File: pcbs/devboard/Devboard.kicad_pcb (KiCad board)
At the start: 2 copper layers, 11 parts, among them J1 Power, J2 Left, J3 ARM-JTAG, J4 Right, J5 JTAG, SW1 SW_Push, U1 Trådfri

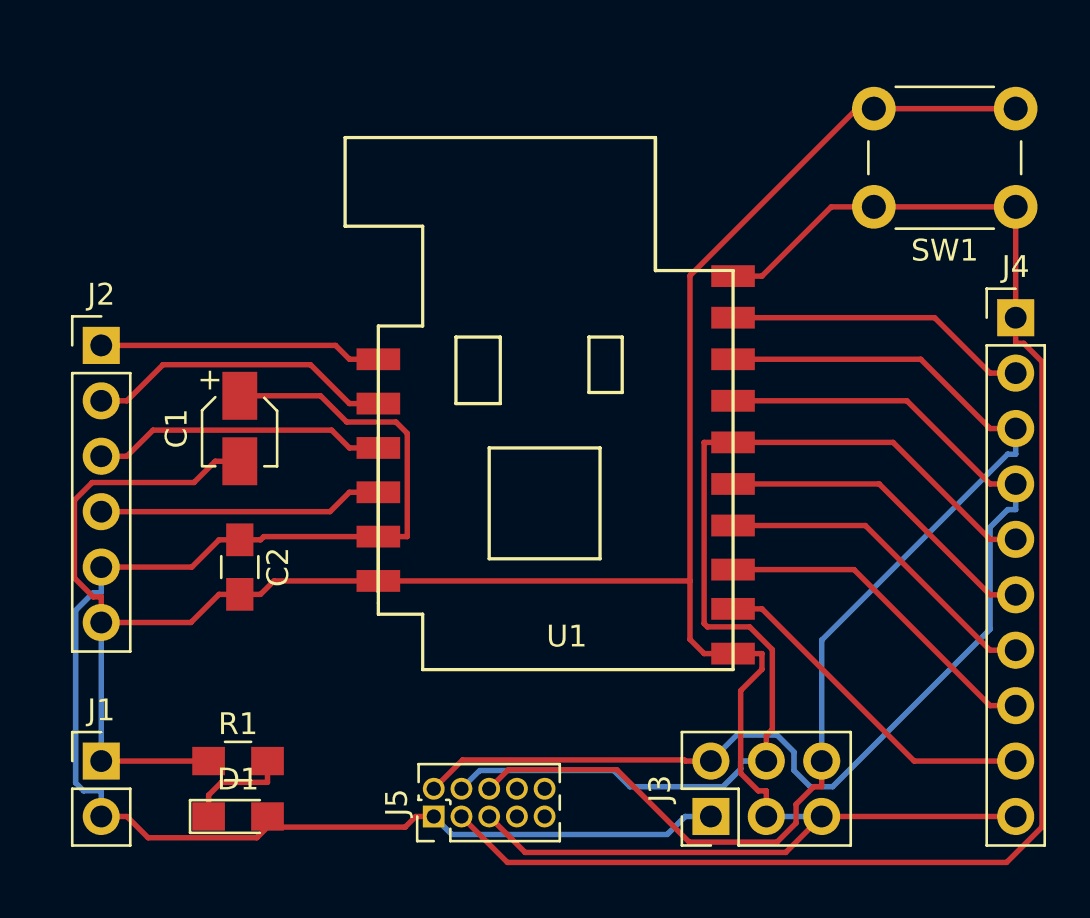
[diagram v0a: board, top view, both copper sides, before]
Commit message: Updated devboard pcb, accidentally swapped GND and VCC line.
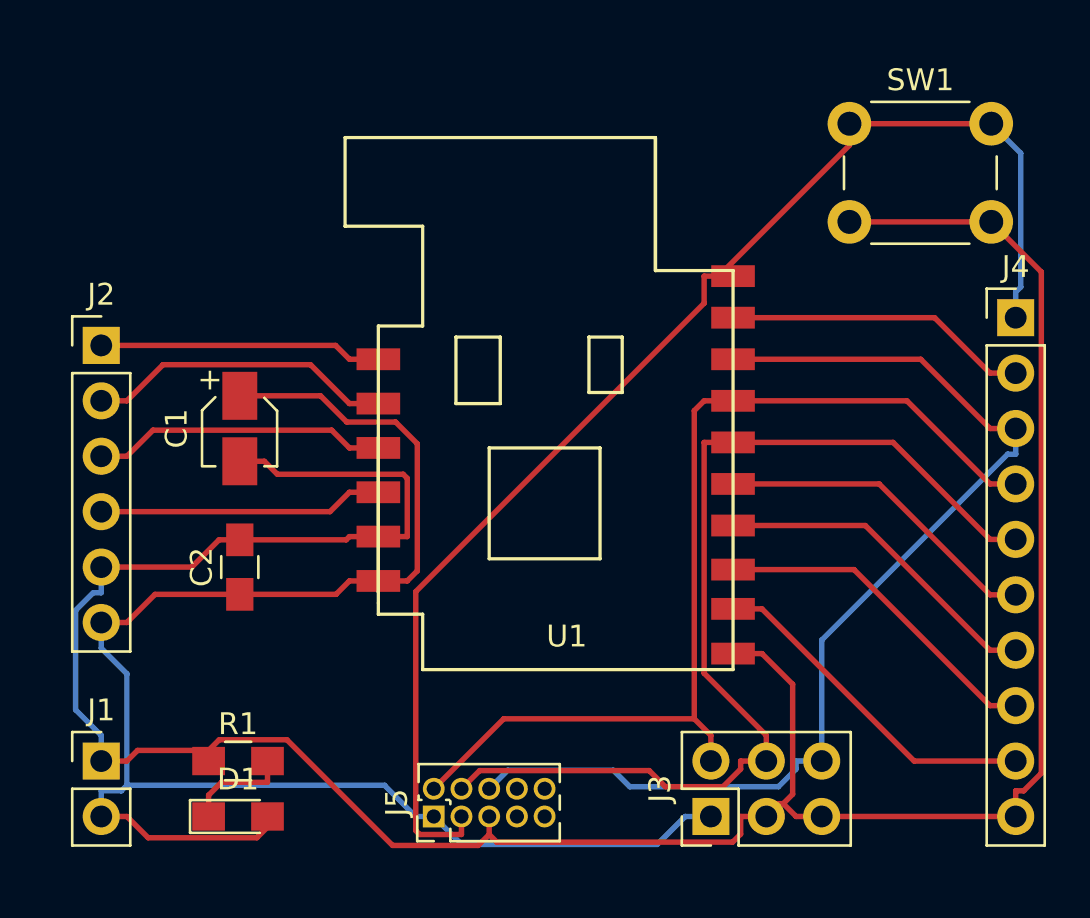
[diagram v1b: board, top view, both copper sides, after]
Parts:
- moved SW1 8.52 mm to (177.8, 95.2), turned to 0 degrees
- turned C2 to 90 degrees
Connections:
- J2 pad 5: +3V3 -> GND
- J2 pad 6: GND -> +3V3
- U1 pad 5: +3V3 -> GND
- U1 pad 6: GND -> +3V3
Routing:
- net /RESETn: track 71.6 -> 60.7 mm
- net +3V3: track 70.7 -> 77.9 mm
- net /SWDIO: track 52.9 -> 46.1 mm
- net /SWO: track 53.1 -> 50.0 mm
- net /SWCLK: track 48.6 -> 47.2 mm
- net GND: track 128.6 -> 127.5 mm

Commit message: Updated PCBs
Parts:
- J3: footprint Pin_Headers:Pin_Header_Straight_2x03_Pitch2.54mm -> Pin_Headers:Pin_Header_Straight_2x05_Pitch1.27mm
- J5: footprint Pin_Headers:Pin_Header_Straight_2x05_Pitch1.27mm -> Pin_Headers:Pin_Header_Straight_2x03_Pitch2.54mm
- U1: value Trådfri -> TRADFRI; footprint Parts:Trådfri PCB2.0 -> IKEA:TRADFRI_PCB2.0
- moved U1 12.0 mm to (166.7, 96.4)
- moved J4 4.44 mm to (181.0, 104.1)
- moved SW1 3.24 mm to (174.6, 94.6)
- moved J3 3.24 mm to (168.3, 126.4)
- moved C1 1.27 mm to (148.6, 109.2)
- moved C2 1.27 mm to (148.6, 115.6)
- moved D1 0.63 mm to (150.4, 127.0)
- moved J5 0.63 mm to (158.1, 127.0)
- moved R1 0.63 mm to (150.4, 124.5)
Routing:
- net GND: track 127.5 -> 110.3 mm
- net +3V3: track 77.9 -> 64.8 mm
- net /RESETn: track 60.7 -> 73.1 mm
- net /SWO: track 50.0 -> 41.5 mm
- net /SWCLK: track 47.2 -> 38.8 mm
- net /SWDIO: track 46.1 -> 42.0 mm
- net Net-(J4-Pad2): track 14.0 -> 10.9 mm
- net Net-(J4-Pad6): track 15.1 -> 12.2 mm
- net Net-(J4-Pad7): track 15.3 -> 12.5 mm
- net Net-(J4-Pad8): track 15.5 -> 12.8 mm
- net Net-(J4-Pad9): track 15.8 -> 13.2 mm
- net Net-(J2-Pad4): track 13.1 -> 10.4 mm
- net Net-(J2-Pad3): track 13.5 -> 11.1 mm
- net Net-(J2-Pad2): track 14.1 -> 11.7 mm
- net Net-(J2-Pad1): track 13.0 -> 10.6 mm
- added copper zone on B.Cu, net GND
- added copper zone on F.Cu, net GND
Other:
- board text added: "https://github.com/ basilfx/TRADFRI-Hacking"

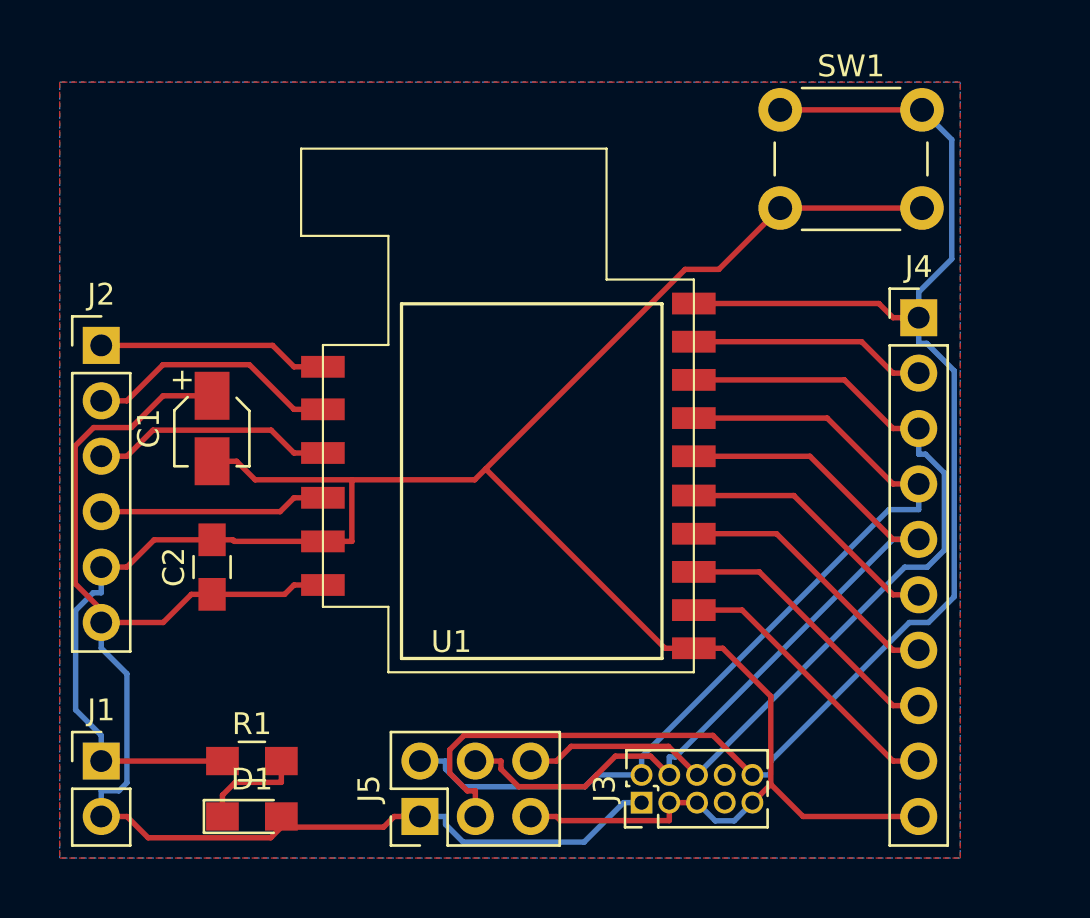
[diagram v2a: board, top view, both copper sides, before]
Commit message: Fixed edge cuts. Upgrade tot Kicad 5.0-rc2.
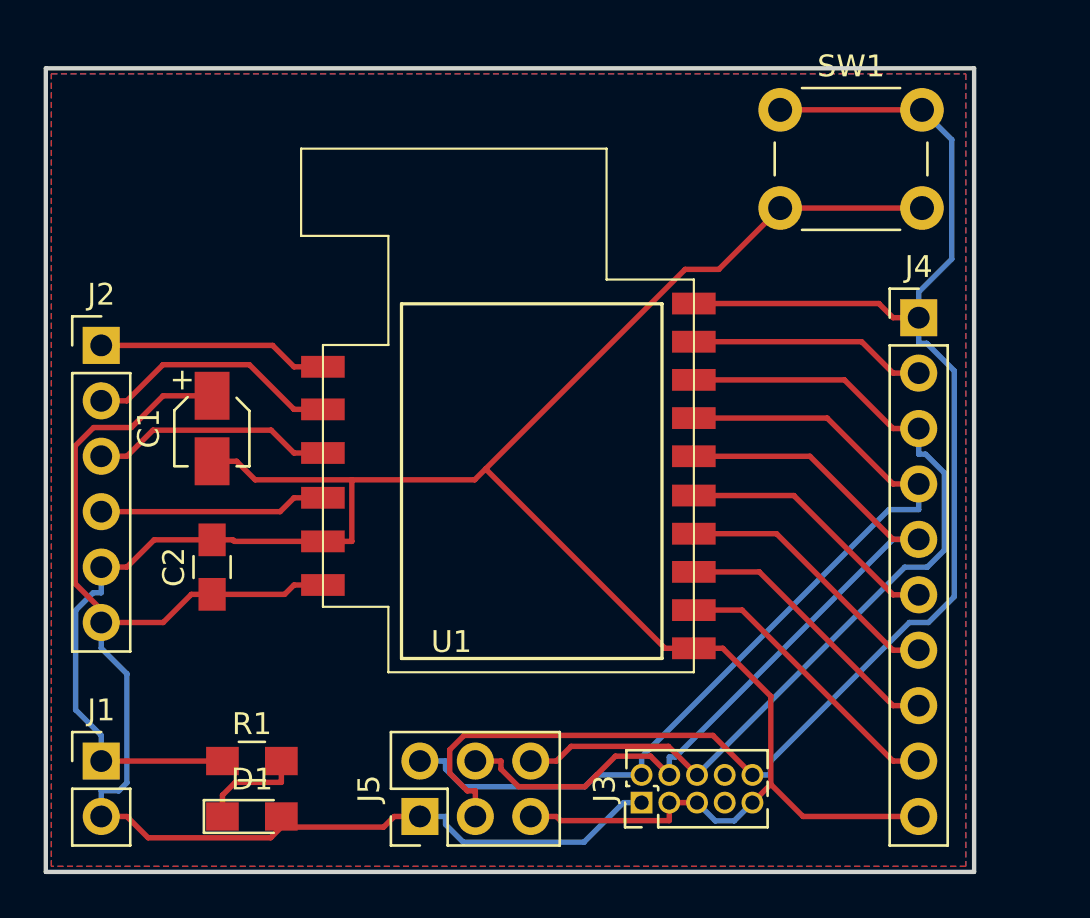
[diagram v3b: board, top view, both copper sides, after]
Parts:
- SW1: value SW_Push -> RESET
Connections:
- J3 pad 7: (no net) -> Net-(J3-Pad7)
- J3 pad 8: (no net) -> Net-(J3-Pad8)
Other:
- board outline added: 42.5 x 36.8 mm
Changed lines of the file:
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@@
-(kicad_pcb (version 4) (host pcbnew 4.0.7)
+(kicad_pcb (version 20171130) (host pcbnew "(5.0.0-rc2-dev-707-g2ed24a4)")
   (general
-    (links 44)
-    (no_connects 0)
-    (area 140.869999 91.64 183.615001 129.739524)
     (thickness 1.6)
     (drawings 5)
@@
     (zones 0)
     (modules 11)
-    (nets 17)
+    (nets 19)
   )
   (page A4)
@@
     (trace_min 0.2)
     (segment_width 0.2)
-    (edge_width 0.15)
+    (edge_width 0.2)
     (via_size 0.6)
     (via_drill 0.4)
@@
       (layerselection 0x00030_80000001)
       (usegerberextensions false)
+      (usegerberattributes false)
+      (usegerberadvancedattributes false)
+      (creategerberjobfile false)
       (excludeedgelayer true)
       (linewidth 0.100000)
@@
       (hpglpenspeed 20)
       (hpglpendiameter 15)
-      (hpglpenoverlay 2)
       (psnegative false)
       (psa4output false)
@@
   (net 15 "Net-(J4-Pad8)")
   (net 16 "Net-(J4-Pad9)")
+  (net 17 "Net-(J3-Pad7)")
+  (net 18 "Net-(J3-Pad8)")
   (net_class Default "Dit is de standaard class."
     (clearance 0.2)
@@
     (add_net "Net-(J2-Pad3)")
     (add_net "Net-(J2-Pad4)")
+    (add_net "Net-(J3-Pad7)")
+    (add_net "Net-(J3-Pad8)")
     (add_net "Net-(J4-Pad2)")
     (add_net "Net-(J4-Pad6)")
@@
       (effects (font (size 1 1) (thickness 0.15)))
     )
-    (fp_text value Left (at 0 15.03) (layer F.Fab)
+    (fp_text value Left (at -0.01 -2.51) (layer F.Fab)
       (effects (font (size 1 1) (thickness 0.15)))
     )
@@
       (effects (font (size 1 1) (thickness 0.15)))
     )
-    (fp_text value Right (at -2.54 21.59 90) (layer F.Fab)
+    (fp_text value Right (at -0.075 -2.74 180) (layer F.Fab)
       (effects (font (size 1 1) (thickness 0.15)))
     )
@@
       (effects (font (size 1 1) (thickness 0.15)))
     )
-    (fp_text value SW_Push (at 3.75 6.7) (layer F.Fab)
+    (fp_text value RESET (at -2.225 2.285 90) (layer F.Fab)
       (effects (font (size 1 1) (thickness 0.15)))
     )
@@
       (net 11 /RESETn))
     (model ${KISYS3DMOD}/Buttons_Switches_THT.3dshapes/SW_PUSH_6mm.wrl
-      (at (xyz 0.005 0 0))
+      (offset (xyz 0.1269999980926514 0 0))
       (scale (xyz 0.3937 0.3937 0.3937))
       (rotate (xyz 0 0 0))
@@
       (effects (font (size 1 1) (thickness 0.15)))
     )
-    (fp_text value ARM-JTAG (at 0.635 6.775 90) (layer F.Fab)
+    (fp_text value ARM-JTAG (at 3.565 2.625 180) (layer F.Fab)
       (effects (font (size 1 1) (thickness 0.15)))
     )
@@
     (pad 6 thru_hole oval (at 1.27 2.54 90) (size 1 1) (drill 0.65) (layers *.Cu *.Mask)
       (net 10 /SWO))
-    (pad 7 thru_hole oval (at 0 3.81 90) (size 1 1) (drill 0.65) (layers *.Cu *.Mask))
-    (pad 8 thru_hole oval (at 1.27 3.81 90) (size 1 1) (drill 0.65) (layers *.Cu *.Mask))
+    (pad 7 thru_hole oval (at 0 3.81 90) (size 1 1) (drill 0.65) (layers *.Cu *.Mask)
+      (net 17 "Net-(J3-Pad7)"))
+    (pad 8 thru_hole oval (at 1.27 3.81 90) (size 1 1) (drill 0.65) (layers *.Cu *.Mask)
+      (net 18 "Net-(J3-Pad8)"))
     (pad 9 thru_hole oval (at 0 5.08 90) (size 1 1) (drill 0.65) (layers *.Cu *.Mask)
       (net 1 GND))
@@
       (effects (font (size 1 1) (thickness 0.15)))
     )
-    (fp_text value JTAG (at 1.27 7.41 90) (layer F.Fab)
+    (fp_text value JTAG (at 5 2.485 180) (layer F.Fab)
       (effects (font (size 1 1) (thickness 0.15)))
     )
@@
     (effects (font (size 1.5 1.5) (thickness 0.3)) (justify mirror))
   )
-  (gr_line (start 183.515 92.71) (end 140.97 92.71) (layer B.CrtYd) (width 0.2))
-  (gr_line (start 183.515 129.54) (end 183.515 92.71) (layer B.CrtYd) (width 0.2))
-  (gr_line (start 140.97 129.54) (end 183.515 129.54) (layer B.CrtYd) (width 0.2))
-  (gr_line (start 140.97 92.71) (end 140.97 129.54) (layer B.CrtYd) (width 0.2))
+  (gr_line (start 183.515 92.71) (end 140.97 92.71) (layer Edge.Cuts) (width 0.2))
+  (gr_line (start 183.515 129.54) (end 183.515 92.71) (layer Edge.Cuts) (width 0.2))
+  (gr_line (start 140.97 129.54) (end 183.515 129.54) (layer Edge.Cuts) (width 0.2))
+  (gr_line (start 140.97 92.71) (end 140.97 129.54) (layer Edge.Cuts) (width 0.2))
   (segment (start 148.59 114.32) (end 149.5403 114.32) (width 0.25) (layer F.Cu) (net 1))
   (segment (start 164.5606 127.1903) (end 169.545 127.1903) (width 0.25) (layer F.Cu) (net 1))
@@
   (segment (start 170.67 117.541) (end 172.8807 117.541) (width 0.25) (layer F.Cu) (net 16))
   (segment (start 180.975 124.46) (end 179.7997 124.46) (width 0.25) (layer F.Cu) (net 16))
-  (zone (net 0) (net_name "") (layer F.Cu) (hatch full 0.508)
+  (zone (net 0) (net_name "") (layers F&B.Cu) (hatch edge 0.508)
     (connect_pads (clearance 0.508))
     (min_thickness 0.254)
@@
     (polygon
       (pts
-        (xy 168.275 93.98) (xy 151.765 93.98) (xy 151.765 101.6) (xy 168.275 101.6)
+        (xy 149.86 92.71) (xy 169.418 92.71) (xy 169.418 101.854) (xy 149.86 101.854)
       )
     )
   )
-  (zone (net 0) (net_name "") (layer B.Cu) (hatch full 0.508)
-    (connect_pads (clearance 0.508))
-    (min_thickness 0.254)
-    (keepout (tracks not_allowed) (vias not_allowed) (copperpour not_allowed))
-    (fill (arc_segments 16) (thermal_gap 0.508) (thermal_bridge_width 0.508))
-    (polygon
-      (pts
-        (xy 151.765 93.98) (xy 168.275 93.98) (xy 168.275 101.6) (xy 151.765 101.6)
-      )
-    )
-  )
-  (zone (net 1) (net_name GND) (layer F.Cu) (hatch full 0.508)
+  (zone (net 1) (net_name GND) (layer F.Cu) (hatch edge 0.508)
     (connect_pads (clearance 0.508))
     (min_thickness 0.254)
@@
     (polygon
       (pts
-        (xy 182.88 128.905) (xy 182.88 93.345) (xy 141.605 93.345) (xy 141.605 128.905)
+        (xy 141.224 92.964) (xy 183.134 92.964) (xy 183.134 129.286) (xy 141.224 129.286)
       )
     )
   )
-  (zone (net 1) (net_name GND) (layer B.Cu) (hatch full 0.508)
+  (zone (net 1) (net_name GND) (layer B.Cu) (hatch edge 0.508)
     (connect_pads (clearance 0.508))
     (min_thickness 0.254)
@@
     (polygon
       (pts
-        (xy 141.605 93.345) (xy 182.88 93.345) (xy 182.88 128.905) (xy 141.605 128.905)
+        (xy 141.224 92.964) (xy 183.134 92.964) (xy 183.134 129.286) (xy 141.224 129.286)
       )
     )
